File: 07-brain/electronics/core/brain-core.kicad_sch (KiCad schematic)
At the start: 8 parts, among them J1 Conn_02x04_Odd_Even, J2 Conn_02x02_Odd_Even, J3 Conn_02x05_Odd_Even

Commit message: Design Brain/Core PCB
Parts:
- removed J1: Conn_02x04_Odd_Even, Connector_PinHeader_2.54mm:PinHeader_2x04_P2.54mm_Vertical, symbol Connector_Generic:Conn_02x04_Odd_Even
- removed J3: Conn_02x05_Odd_Even, Connector_PinHeader_2.54mm:PinHeader_2x05_P2.54mm_Vertical, symbol Connector_Generic:Conn_02x05_Odd_Even
- added #J8: Conn_01x02, Connector_PinHeader_2.54mm:PinHeader_1x02_P2.54mm_Vertical, symbol Connector_Generic:Conn_01x02
- added J1, J8: Conn_02x03_Odd_Even, Connector_PinHeader_2.54mm:PinHeader_2x03_P2.54mm_Vertical, symbol Connector_Generic:Conn_02x03_Odd_Even
- added J3: Conn_02x02_Odd_Even, Connector_PinHeader_2.54mm:PinHeader_2x02_P2.54mm_Vertical, symbol Connector_Generic:Conn_02x02_Odd_Even
- added J7: Conn_02x05_Odd_Even, Connector_PinHeader_2.54mm:PinHeader_2x05_P2.54mm_Vertical, symbol Connector_Generic:Conn_02x05_Odd_Even
- NT1: footprint (none) -> NetTie:NetTie-2_SMD_Pad2.0mm
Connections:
- net AUDIO_CV_IN_1: now also J7.10 (Pin_10)
- net AUDIO_CV_IN_2: now also J7.6 (Pin_6)
- net AUDIO_CV_OUT_1: now also J8.5 (Pin_5)
- net AUDIO_CV_OUT_2: now also J8.2 (Pin_2)
- net BTN_1: now also J3.3 (Pin_3)
- net BTN_2: now also J3.1 (Pin_1)
- net BTN_LED_1: now also J3.2 (Pin_2)
- net BTN_LED_2: now also J3.4 (Pin_4)
- net GND: now also J7.2 (Pin_2), J7.4 (Pin_4), J7.7 (Pin_7), J7.8 (Pin_8), J7.9 (Pin_9), J8.1 (Pin_1), J8.3 (Pin_3), J8.4 (Pin_4), J8.6 (Pin_6)
- net LED_1: now also J1.5 (Pin_5)
- net LED_2: now also J1.3 (Pin_3)
- net LED_3: now also J1.1 (Pin_1)
- net LED_4: now also J1.2 (Pin_2)
- net LED_5: now also J1.4 (Pin_4)
- net LED_6: now also J1.6 (Pin_6)
- net MCU/UART_RX: now also #J8.2 (Pin_2)
- net MCU/UART_TX: now also #J8.1 (Pin_1)
- net MIDI_4R: now also J2.3 (Pin_3)
- net MIDI_5T: now also J2.1 (Pin_1)
- net POT_1: now also J7.5 (Pin_5)
- net POT_2: now also J7.3 (Pin_3)
- net POT_3: now also J7.1 (Pin_1)
- net PULSE_IN: now also J2.2 (Pin_2)
- net PULSE_OUT: now also J2.4 (Pin_4)
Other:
- sheet MCU ports: added none; removed SWCLK, SWDIO
- note added: "2"
- note added: "3"
- note added: "4"
- note added: "6"
- moved on the sheet: J2

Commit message: Brain PCB WIP
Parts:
- removed NT1: NetTie_2, NetTie:NetTie-2_SMD_Pad2.0mm, symbol Device:NetTie_2
- added J10: Conn_01x02, Connector_PinHeader_2.54mm:PinHeader_1x02_P2.54mm_Vertical, symbol Connector_Generic:Conn_01x02
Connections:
- new net +12V: J10.1 (Pin_1)
- new net +3.3V: J10.2 (Pin_2)
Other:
- moved on the sheet: J8

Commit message: Designed Brain UI PCB
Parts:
- added J_USB_C_BRKOUT1: Conn_01x05, Connector_PinHeader_2.54mm:PinHeader_1x05_P2.54mm_Vertical, symbol Connector_Generic:Conn_01x05
- added SW1: SW_SPST, Button_Switch_THT:SW_Tactile_SKHH_Angled, symbol Switch:SW_SPST
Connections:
- net AUDIO_CV_IN_1: now also J7.6 (Pin_6); no longer J7.10 (Pin_10)
- net AUDIO_CV_IN_2: now also J7.10 (Pin_10); no longer J7.6 (Pin_6)
- net BTN_1: now also J3.1 (Pin_1); no longer J3.3 (Pin_3)
- net BTN_2: now also J3.3 (Pin_3); no longer J3.1 (Pin_1)
- net BTN_LED_1: now also J3.4 (Pin_4); no longer J3.2 (Pin_2)
- net BTN_LED_2: now also J3.2 (Pin_2); no longer J3.4 (Pin_4)
- net GND: now also J7.5 (Pin_5), SW1.2 (B); no longer J7.2 (Pin_2)
- net LED_1: now also J1.1 (Pin_1); no longer J1.5 (Pin_5)
- net LED_3: now also J1.5 (Pin_5); no longer J1.1 (Pin_1)
- net LED_4: now also J1.6 (Pin_6); no longer J1.2 (Pin_2)
- net LED_6: now also J1.2 (Pin_2); no longer J1.6 (Pin_6)
- net POT_1: now also J7.3 (Pin_3); no longer J7.5 (Pin_5)
- net POT_2: now also J7.1 (Pin_1); no longer J7.3 (Pin_3)
- net POT_3: now also J7.2 (Pin_2); no longer J7.1 (Pin_1)
- no-connect marks 0 -> 6

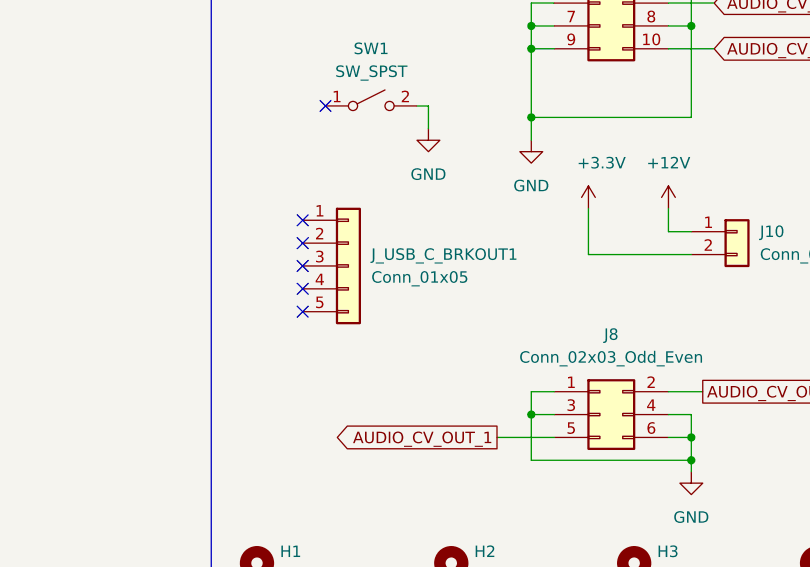
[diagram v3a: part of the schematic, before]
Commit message: Added decoupling caps to DAC in Brain
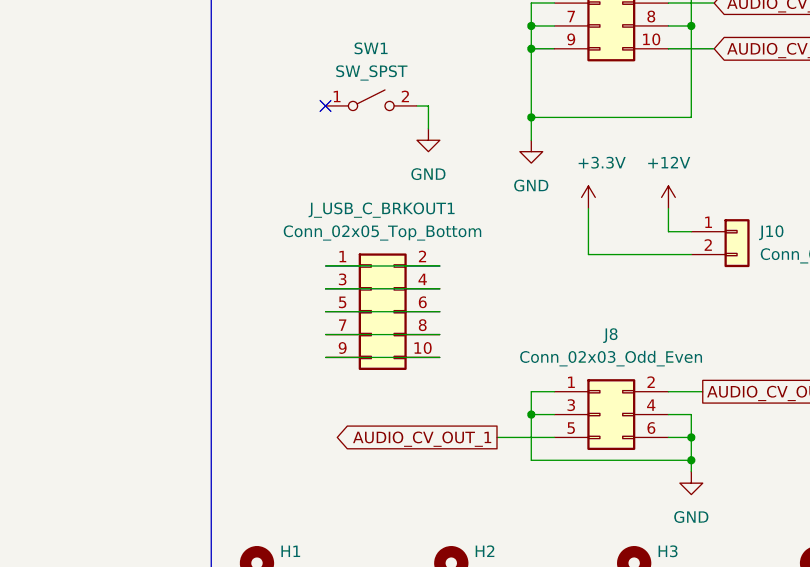
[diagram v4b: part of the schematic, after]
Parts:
- removed J_USB_C_BRKOUT1: Conn_01x05, Connector_PinHeader_2.54mm:PinHeader_1x05_P2.54mm_Vertical, symbol Connector_Generic:Conn_01x05
- added J_USB_C_BRKOUT1: Conn_02x05_Top_Bottom, Connector_PinHeader_2.54mm:PinHeader_2x05_P2.54mm_Vertical, symbol Connector_Generic:Conn_02x05_Odd_Even
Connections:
- new net: J_USB_C_BRKOUT1.1 (Pin_1), J_USB_C_BRKOUT1.2 (Pin_2)
- new net: J_USB_C_BRKOUT1.10 (Pin_10), J_USB_C_BRKOUT1.9 (Pin_9)
- new net: J_USB_C_BRKOUT1.3 (Pin_3), J_USB_C_BRKOUT1.4 (Pin_4)
- new net: J_USB_C_BRKOUT1.5 (Pin_5), J_USB_C_BRKOUT1.6 (Pin_6)
- new net: J_USB_C_BRKOUT1.7 (Pin_7), J_USB_C_BRKOUT1.8 (Pin_8)
- no-connect marks 6 -> 1
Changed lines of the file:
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@@
-	)
-	(no_connect
-		(at 247.65 132.08)
-	)
-	(no_connect
-		(at 247.65 124.46)
 	)
 	(no_connect
 		(at 250.19 109.22)
 	)
-	(no_connect
-		(at 247.65 127)
-	)
-	(no_connect
-		(at 247.65 121.92)
-	)
-	(no_connect
-		(at 247.65 129.54)
-	)
 	(polyline
 		(pts
@@
 	(wire
 		(pts
+			(xy 250.19 132.08) (xy 262.89 132.08)
+		)
+		(stroke
+			(width 0)
+			(type default)
+		)
+	)
+	(wire
+		(pts
 			(xy 88.9 81.28) (xy 101.6 81.28)
 		)
@@
 	(wire
 		(pts
+			(xy 250.19 134.62) (xy 262.89 134.62)
+		)
+		(stroke
+			(width 0)
+			(type default)
+		)
+	)
+	(wire
+		(pts
 			(xy 52.07 83.82) (xy 54.61 83.82)
 		)
@@
 	(wire
 		(pts
+			(xy 250.19 129.54) (xy 262.89 129.54)
+		)
+		(stroke
+			(width 0)
+			(type default)
+		)
+	)
+	(wire
+		(pts
 			(xy 88.9 118.11) (xy 101.6 118.11)
 		)
@@
 	(wire
 		(pts
+			(xy 250.19 127) (xy 262.89 127)
+		)
+		(stroke
+			(width 0)
+			(type default)
+		)
+	)
+	(wire
+		(pts
 			(xy 273.05 102.87) (xy 273.05 110.49)
 		)
@@
 		(pts
 			(xy 271.78 77.47) (xy 275.59 77.47)
+		)
+		(stroke
+			(width 0)
+			(type default)
+		)
+	)
+	(wire
+		(pts
+			(xy 250.19 137.16) (xy 262.89 137.16)
 		)
 		(stroke
@@
 	)
 	(symbol
-		(lib_id "Connector_Generic:Conn_01x05")
-		(at 252.73 127 0)
-		(unit 1)
-		(exclude_from_sim no)
-		(in_bom yes)
-		(on_board yes)
-		(dnp no)
-		(fields_autoplaced yes)
-		(property "Reference" "J_USB_C_BRKOUT1"
-			(at 255.27 125.7299 0)
-			(effects
-				(font
-					(size 1.27 1.27)
-				)
-				(justify left)
-			)
-		)
-		(property "Value" "Conn_01x05"
-			(at 255.27 128.2699 0)
-			(effects
-				(font
-					(size 1.27 1.27)
-				)
-				(justify left)
-			)
-		)
-		(property "Footprint" "Connector_PinHeader_2.54mm:PinHeader_1x05_P2.54mm_Vertical"
-			(at 252.73 127 0)
-			(effects
-				(font
-					(size 1.27 1.27)
-				)
-				(hide yes)
-			)
-		)
-		(property "Datasheet" "~"
-			(at 252.73 127 0)
-			(effects
-				(font
-					(size 1.27 1.27)
-				)
-				(hide yes)
-			)
-		)
-		(property "Description" "Generic connector, single row, 01x05, script generated (kicad-library-utils/schlib/autogen/connector/)"
-			(at 252.73 127 0)
-			(effects
-				(font
-					(size 1.27 1.27)
-				)
-				(hide yes)
-			)
-		)
-		(property "Part No." ""
-			(at 252.73 127 0)
-			(effects
-				(font
-					(size 1.27 1.27)
-				)
-				(hide yes)
-			)
-		)
-		(property "Part URL" ""
-			(at 252.73 127 0)
-			(effects
-				(font
-					(size 1.27 1.27)
-				)
-				(hide yes)
-			)
-		)
-		(property "Vendor" ""
-			(at 252.73 127 0)
-			(effects
-				(font
-					(size 1.27 1.27)
-				)
-				(hide yes)
-			)
-		)
-		(property "LCSC" ""
-			(at 252.73 127 0)
-			(effects
-				(font
-					(size 1.27 1.27)
-				)
-				(hide yes)
-			)
-		)
-		(pin "1"
-		)
-		(pin "2"
-		)
-		(pin "3"
-		)
-		(pin "4"
-		)
-		(pin "5"
-		)
-		(instances
-			(project ""
-				(path "/8e2e31f3-eed5-4de1-966c-f4162758c735"
-					(reference "J_USB_C_BRKOUT1")
-					(unit 1)
-				)
-			)
-		)
-	)
-	(symbol
 		(lib_id "Mechanical:MountingHole")
 		(at 264.16 160.02 0)
@@
 					(unit 1)
 				)
+			)
+		)
+	)
+	(symbol
+		(lib_id "Connector_Generic:Conn_02x05_Odd_Even")
+		(at 255.27 132.08 0)
+		(unit 1)
+		(exclude_from_sim no)
+		(in_bom yes)
+		(on_board yes)
+		(dnp no)
+		(fields_autoplaced yes)
+		(property "Reference" "J_USB_C_BRKOUT1"
+			(at 256.54 120.65 0)
+			(effects
+				(font
+					(size 1.27 1.27)
+				)
+			)
+		)
+		(property "Value" "Conn_02x05_Top_Bottom"
+			(at 256.54 123.19 0)
+			(effects
+				(font
+					(size 1.27 1.27)
+				)
+			)
+		)
+		(property "Footprint" "Connector_PinHeader_2.54mm:PinHeader_2x05_P2.54mm_Vertical"
+			(at 255.27 132.08 0)
+			(effects
+				(font
+					(size 1.27 1.27)
+				)
+				(hide yes)
+			)
+		)
+		(property "Datasheet" "~"
+			(at 255.27 132.08 0)
+			(effects
+				(font
+					(size 1.27 1.27)
+				)
+				(hide yes)
+			)
+		)
+		(property "Description" "Generic connector, double row, 02x05, odd/even pin numbering scheme (row 1 odd numbers, row 2 even numbers), script generated (kicad-library-utils/schlib/autogen/connector/)"
+			(at 255.27 132.08 0)
+			(effects
+				(font
+					(size 1.27 1.27)
+				)
+				(hide yes)
+			)
+		)
+		(property "Part No." ""
+			(at 255.27 132.08 0)
+			(effects
+				(font
+					(size 1.27 1.27)
+				)
+				(hide yes)
+			)
+		)
+		(property "Part URL" ""
+			(at 255.27 132.08 0)
+			(effects
+				(font
+					(size 1.27 1.27)
+				)
+				(hide yes)
+			)
+		)
+		(property "Vendor" ""
+			(at 255.27 132.08 0)
+			(effects
+				(font
+					(size 1.27 1.27)
+				)
+				(hide yes)
+			)
+		)
+		(property "LCSC" ""
+			(at 255.27 132.08 0)
+			(effects
+				(font
+					(size 1.27 1.27)
+				)
+				(hide yes)
+			)
+		)
+		(pin "1"
+		)
+		(pin "2"
+		)
+		(pin "3"
+		)
+		(pin "4"
+		)
+		(pin "5"
+		)
+		(pin "6"
+		)
+		(pin "7"
+		)
+		(pin "8"
+		)
+		(pin "9"
+		)
+		(pin "10"
+		)
+		(instances
+			(project ""
+				(path "/8e2e31f3-eed5-4de1-966c-f4162758c735"
+					(reference "J_USB_C_BRKOUT1")
+					(unit 1)
+				)

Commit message: Refined Brain PCBs
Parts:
- added J9: Conn_01x02, Connector_PinHeader_2.54mm:PinHeader_1x02_P2.54mm_Vertical, symbol Connector_Generic:Conn_01x02
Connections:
- net +12V: now also J9.1 (Pin_1), J9.2 (Pin_2)
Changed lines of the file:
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@@
 	)
 	(junction
+		(at 299.72 115.57)
+		(diameter 0)
+		(color 0 0 0 0)
+	)
+	(junction
 		(at 273.05 143.51)
 		(diameter 0)
@@
 		)
 	)
+	(wire
+		(pts
+			(xy 299.72 115.57) (xy 299.72 118.11)
+		)
+		(stroke
+			(width 0)
+			(type default)
+		)
+	)
 	(polyline
 		(pts
@@
 	(wire
 		(pts
+			(xy 299.72 113.03) (xy 299.72 115.57)
+		)
+		(stroke
+			(width 0)
+			(type default)
+		)
+	)
+	(wire
+		(pts
 			(xy 260.35 109.22) (xy 261.62 109.22)
 		)
@@
 	(wire
 		(pts
+			(xy 299.72 115.57) (xy 303.53 115.57)
+		)
+		(stroke
+			(width 0)
+			(type default)
+		)
+	)
+	(wire
+		(pts
 			(xy 250.19 137.16) (xy 262.89 137.16)
 		)
@@
 	(wire
 		(pts
+			(xy 299.72 118.11) (xy 303.53 118.11)
+		)
+		(stroke
+			(width 0)
+			(type default)
+		)
+	)
+	(wire
+		(pts
 			(xy 288.29 95.25) (xy 290.83 95.25)
 		)
@@
 	(symbol
 		(lib_id "power:+12V")
+		(at 299.72 113.03 0)
+		(unit 1)
+		(exclude_from_sim no)
+		(in_bom yes)
+		(on_board yes)
+		(dnp no)
+		(fields_autoplaced yes)
+		(property "Reference" "#PWR067"
+			(at 299.72 116.84 0)
+			(effects
+				(font
+					(size 1.27 1.27)
+				)
+				(hide yes)
+			)
+		)
+		(property "Value" "+12V"
+			(at 299.72 107.95 0)
+			(effects
+				(font
+					(size 1.27 1.27)
+				)
+			)
+		)
+		(property "Footprint" ""
+			(at 299.72 113.03 0)
+			(effects
+				(font
+					(size 1.27 1.27)
+				)
+				(hide yes)
+			)
+		)
+		(property "Datasheet" ""
+			(at 299.72 113.03 0)
+			(effects
+				(font
+					(size 1.27 1.27)
+				)
+				(hide yes)
+			)
+		)
+		(property "Description" "Power symbol creates a global label with name \"+12V\""
+			(at 299.72 113.03 0)
+			(effects
+				(font
+					(size 1.27 1.27)
+				)
+				(hide yes)
+			)
+		)
+		(pin "1"
+		)
+		(instances
+			(project "brain-core"
+				(path "/8e2e31f3-eed5-4de1-966c-f4162758c735"
+					(reference "#PWR067")
+					(unit 1)
+				)
+			)
+		)
+	)
+	(symbol
+		(lib_id "power:+12V")
 		(at 288.29 120.65 0)
 		(unit 1)
@@
 					(unit 1)
 				)
+			)
+		)
+	)
+	(symbol
+		(lib_id "Connector_Generic:Conn_01x02")
+		(at 308.61 115.57 0)
+		(unit 1)
+		(exclude_from_sim no)
+		(in_bom yes)
+		(on_board yes)
+		(dnp no)
+		(fields_autoplaced yes)
+		(property "Reference" "J9"
+			(at 311.15 115.5699 0)
+			(effects
+				(font
+					(size 1.27 1.27)
+				)
+				(justify left)
+			)
+		)
+		(property "Value" "Conn_01x02"
+			(at 311.15 118.1099 0)
+			(effects
+				(font
+					(size 1.27 1.27)
+				)
+				(justify left)
+			)
+		)
+		(property "Footprint" "Connector_PinHeader_2.54mm:PinHeader_1x02_P2.54mm_Vertical"
+			(at 308.61 115.57 0)
+			(effects
+				(font
+					(size 1.27 1.27)
+				)
+				(hide yes)
+			)
+		)
+		(property "Datasheet" "~"
+			(at 308.61 115.57 0)
+			(effects
+				(font
+					(size 1.27 1.27)
+				)
+				(hide yes)
+			)
+		)
+		(property "Description" "Generic connector, single row, 01x02, script generated (kicad-library-utils/schlib/autogen/connector/)"
+			(at 308.61 115.57 0)
+			(effects
+				(font
+					(size 1.27 1.27)
+				)
+				(hide yes)
+			)
+		)
+		(property "Part No." ""
+			(at 308.61 115.57 0)
+			(effects
+				(font
+					(size 1.27 1.27)
+				)
+				(hide yes)
+			)
+		)
+		(property "Part URL" ""
+			(at 308.61 115.57 0)
+			(effects
+				(font
+					(size 1.27 1.27)
+				)
+				(hide yes)
+			)
+		)
+		(property "Vendor" ""
+			(at 308.61 115.57 0)
+			(effects
+				(font
+					(size 1.27 1.27)
+				)
+				(hide yes)
+			)
+		)
+		(property "LCSC" ""
+			(at 308.61 115.57 0)
+			(effects
+				(font
+					(size 1.27 1.27)
+				)
+				(hide yes)
+			)
+		)
+		(pin "1"
+		)
+		(pin "2"
+		)
+		(instances
+			(project "brain-core"
+				(path "/8e2e31f3-eed5-4de1-966c-f4162758c735"
+					(reference "J9")
+					(unit 1)
+				)

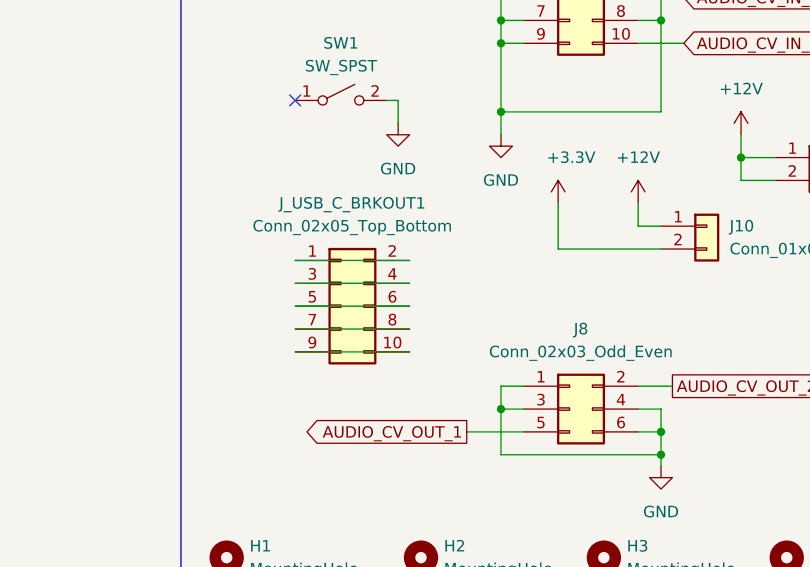
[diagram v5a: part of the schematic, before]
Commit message: Added Adafruit USB-C breakout
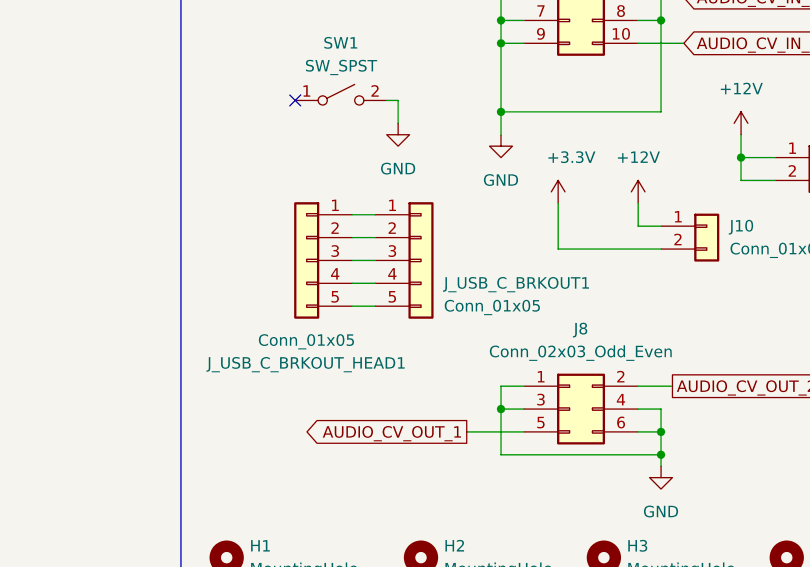
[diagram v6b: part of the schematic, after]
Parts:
- removed J_USB_C_BRKOUT1: Conn_02x05_Top_Bottom, Connector_PinHeader_2.54mm:PinHeader_2x05_P2.54mm_Vertical, symbol Connector_Generic:Conn_02x05_Odd_Even
- added J_USB_C_BRKOUT1: Conn_01x05, Shmoergh_Custom_Footprints:Adafruit 5978 USB-C Breakout, symbol Connector_Generic:Conn_01x05
- added J_USB_C_BRKOUT_HEAD1: Conn_01x05, Connector_PinHeader_2.54mm:PinHeader_1x05_P2.54mm_Vertical, symbol Connector_Generic:Conn_01x05
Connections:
- new net: J_USB_C_BRKOUT1.1 (Pin_1), J_USB_C_BRKOUT_HEAD1.1 (Pin_1)
- new net: J_USB_C_BRKOUT1.2 (Pin_2), J_USB_C_BRKOUT_HEAD1.2 (Pin_2)
- new net: J_USB_C_BRKOUT1.3 (Pin_3), J_USB_C_BRKOUT_HEAD1.3 (Pin_3)
- new net: J_USB_C_BRKOUT1.4 (Pin_4), J_USB_C_BRKOUT_HEAD1.4 (Pin_4)
- new net: J_USB_C_BRKOUT1.5 (Pin_5), J_USB_C_BRKOUT_HEAD1.5 (Pin_5)

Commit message: Brain core PCB design WIP
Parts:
- added J11: Conn_01x01, Connector_PinHeader_2.54mm:PinHeader_1x01_P2.54mm_Vertical, symbol Connector_Generic:Conn_01x01
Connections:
- net at SW1.1 (A): now also J11.1 (Pin_1)
- no-connect marks 1 -> 0
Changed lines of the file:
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@@
 		(color 0 0 0 0)
 	)
-	(no_connect
-		(at 250.19 109.22)
-	)
 	(polyline
 		(pts
@@
 					(unit 1)
 				)
+			)
+		)
+	)
+	(symbol
+		(lib_id "Connector_Generic:Conn_01x01")
+		(at 245.11 109.22 180)
+		(unit 1)
+		(exclude_from_sim no)
+		(in_bom yes)
+		(on_board yes)
+		(dnp no)
+		(fields_autoplaced yes)
+		(property "Reference" "J11"
+			(at 245.11 102.87 0)
+			(effects
+				(font
+					(size 1.27 1.27)
+				)
+			)
+		)
+		(property "Value" "Conn_01x01"
+			(at 245.11 105.41 0)
+			(effects
+				(font
+					(size 1.27 1.27)
+				)
+			)
+		)
+		(property "Footprint" "Connector_PinHeader_2.54mm:PinHeader_1x01_P2.54mm_Vertical"
+			(at 245.11 109.22 0)
+			(effects
+				(font
+					(size 1.27 1.27)
+				)
+				(hide yes)
+			)
+		)
+		(property "Datasheet" "~"
+			(at 245.11 109.22 0)
+			(effects
+				(font
+					(size 1.27 1.27)
+				)
+				(hide yes)
+			)
+		)
+		(property "Description" "Generic connector, single row, 01x01, script generated (kicad-library-utils/schlib/autogen/connector/)"
+			(at 245.11 109.22 0)
+			(effects
+				(font
+					(size 1.27 1.27)
+				)
+				(hide yes)
+			)
+		)
+		(property "Part No." ""
+			(at 245.11 109.22 0)
+			(effects
+				(font
+					(size 1.27 1.27)
+				)
+				(hide yes)
+			)
+		)
+		(property "Part URL" ""
+			(at 245.11 109.22 0)
+			(effects
+				(font
+					(size 1.27 1.27)
+				)
+				(hide yes)
+			)
+		)
+		(property "Vendor" ""
+			(at 245.11 109.22 0)
+			(effects
+				(font
+					(size 1.27 1.27)
+				)
+				(hide yes)
+			)
+		)
+		(property "LCSC" ""
+			(at 245.11 109.22 0)
+			(effects
+				(font
+					(size 1.27 1.27)
+				)
+				(hide yes)
+			)
+		)
+		(pin "1"
+		)
+		(instances
+			(project ""
+				(path "/8e2e31f3-eed5-4de1-966c-f4162758c735"
+					(reference "J11")
+					(unit 1)
+				)

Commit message: Updated USB-C breakout on Brain Core
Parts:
- removed J11: Conn_01x01, Connector_PinHeader_2.54mm:PinHeader_1x01_P2.54mm_Vertical, symbol Connector_Generic:Conn_01x01
- removed J_USB_C_BRKOUT1: Conn_01x05, Shmoergh_Custom_Footprints:Adafruit 5978 USB-C Breakout, symbol Connector_Generic:Conn_01x05
- removed J_USB_C_BRKOUT_HEAD1: Conn_01x05, Connector_PinHeader_2.54mm:PinHeader_1x05_P2.54mm_Vertical, symbol Connector_Generic:Conn_01x05
- removed SW1: SW_SPST, Button_Switch_THT:SW_Tactile_SKHH_Angled, symbol Switch:SW_SPST
